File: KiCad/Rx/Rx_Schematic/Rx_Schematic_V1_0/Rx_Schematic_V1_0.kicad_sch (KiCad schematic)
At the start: 5 parts, among them J1 Analog, J2 Digital

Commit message: Updated schematic
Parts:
- removed J1: Analog, Connector_PinHeader_2.54mm:PinHeader_1x17_P2.54mm_Vertical, symbol Connector_Generic:Conn_01x17
- removed J2: Digital, Connector_PinHeader_2.54mm:PinHeader_1x17_P2.54mm_Vertical, symbol Connector_Generic:Conn_01x17
- added U?: ProMicro, symbol promicro:ProMicro
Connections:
- net at U?.1 (GND): now also U?.1 (GND), U?.23 (GND)
- net at U?.2 (VO): now also U?.2 (VCC)
- net at U?.3 (VI): now also U?.19 (F5)
- net at U?.3 (CE): now also U?.18 (F6)
- net at U?.4 (~{CSN}): now also U?.17 (F7)
- net at U?.5 (SCK): now also U?.16 (B1)
- net at U?.6 (MOSI): now also U?.14 (B2)
- net at U?.7 (MISO): now also U?.15 (B3)
- no-connect marks 2 -> 0
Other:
- moved on the sheet: U?

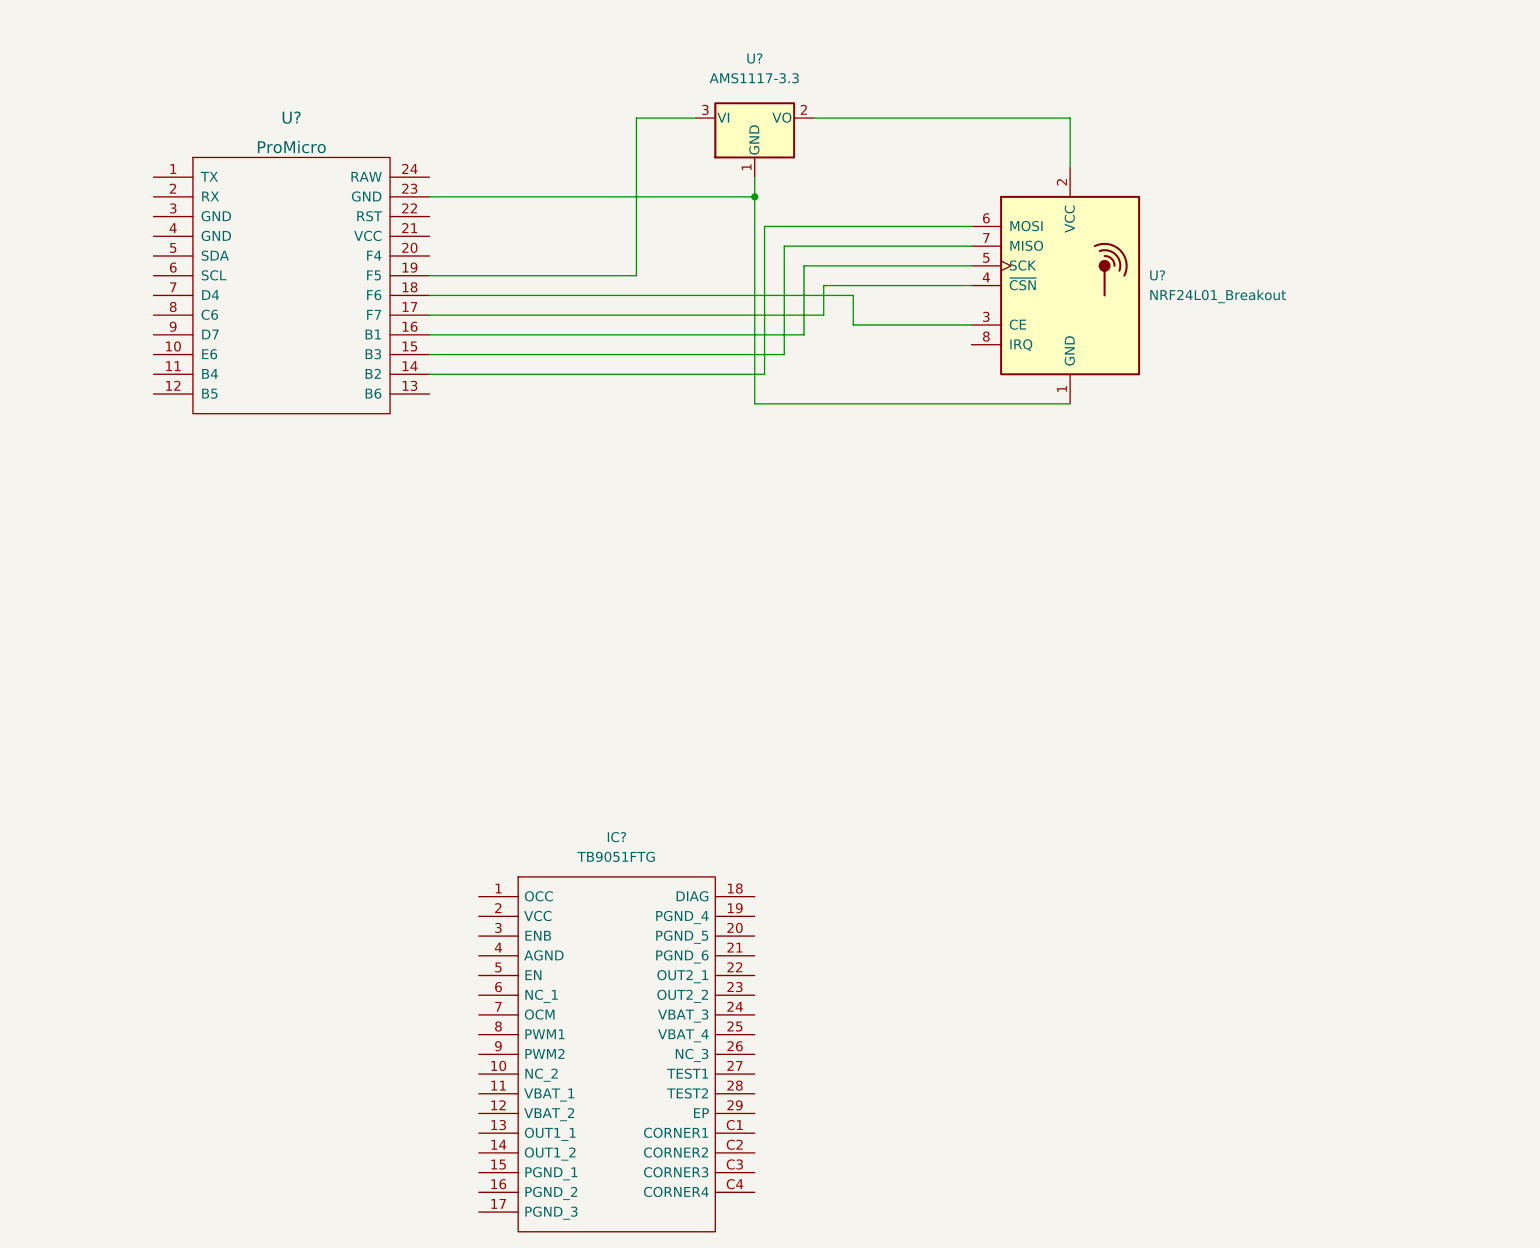
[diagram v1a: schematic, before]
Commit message: Updated Rx schematic
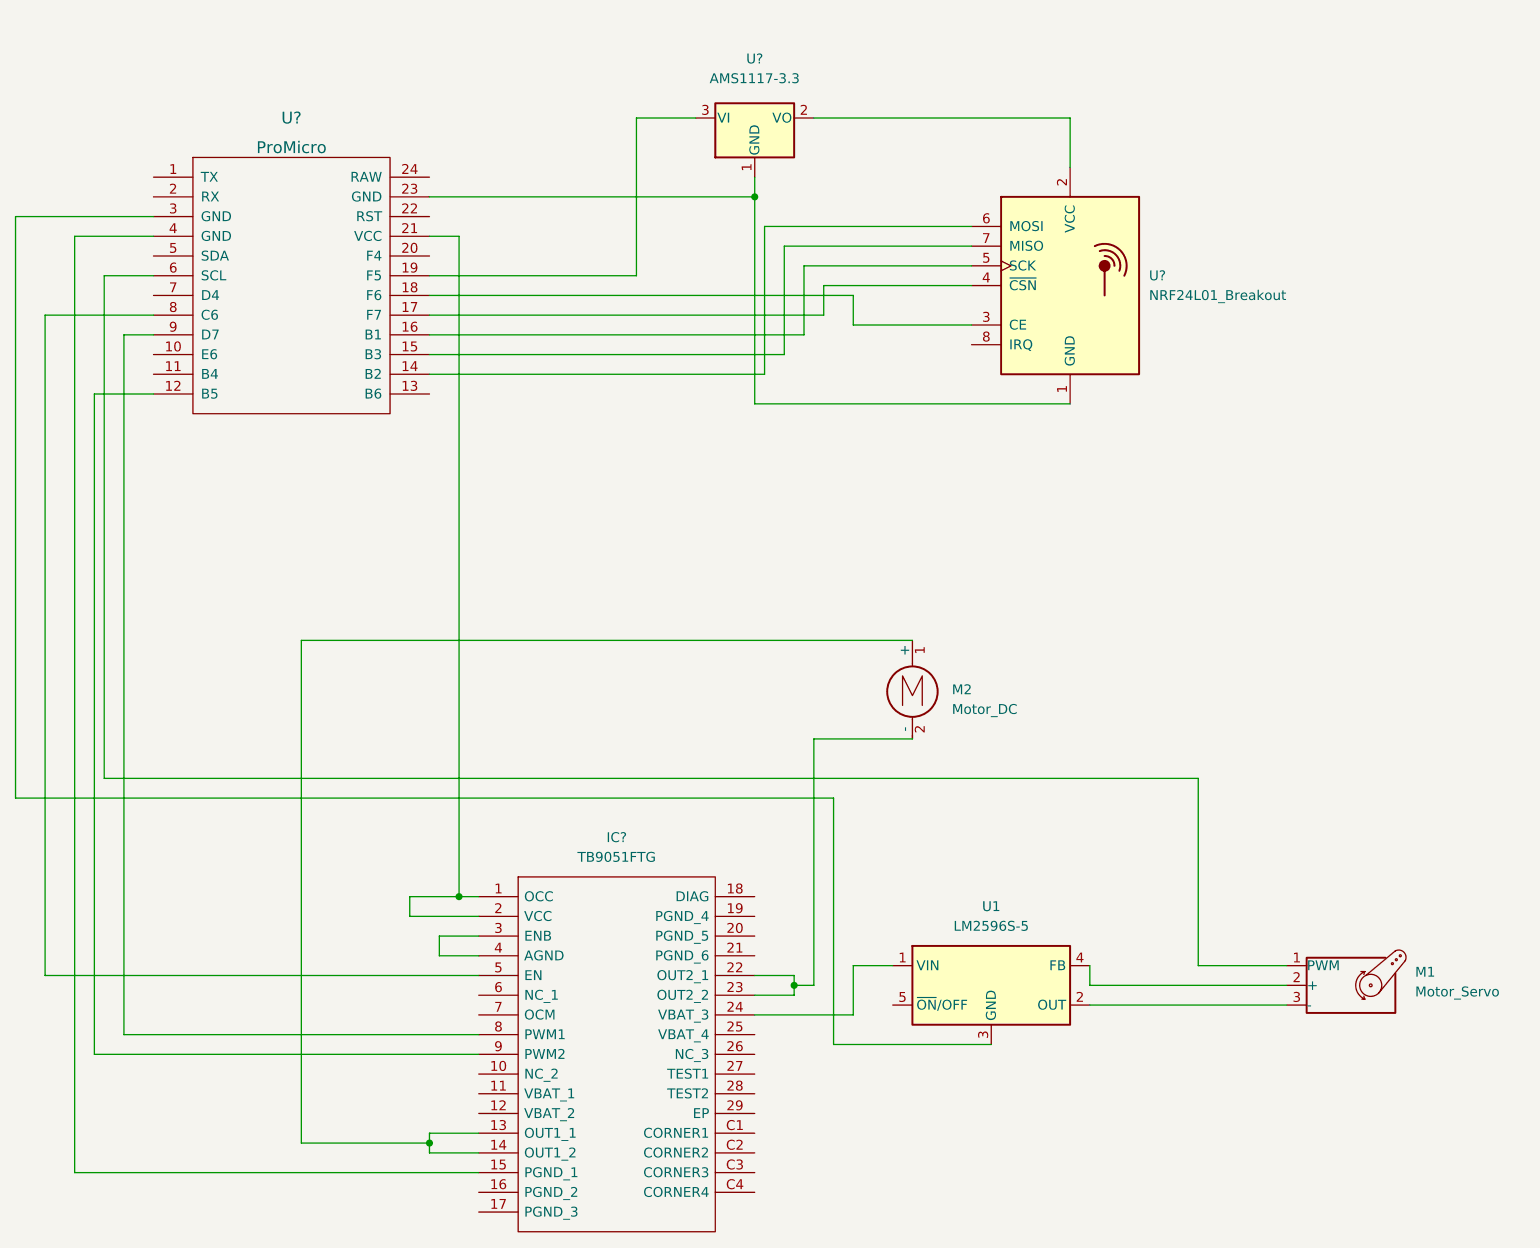
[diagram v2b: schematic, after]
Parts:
- added M1: Motor_Servo, symbol Motor:Motor_Servo
- added M2: Motor_DC, symbol Motor:Motor_DC
- added U1: LM2596S-5, Package_TO_SOT_SMD:TO-263-5_TabPin3, symbol Regulator_Switching:LM2596S-5
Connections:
- net at U?.12 (B5): now also IC?.9 (PWM2)
- net at U?.21 (VCC): now also IC?.1 (OCC), IC?.2 (VCC)
- net at U?.3 (GND): now also U1.3 (GND)
- net at U?.4 (GND): now also IC?.15 (PGND_1)
- net at U?.6 (SCL): now also M1.1 (PWM)
- net at U?.8 (C6): now also IC?.5 (EN)
- net at U?.9 (D7): now also IC?.8 (PWM1)
- net at IC?.13 (OUT1_1): now also IC?.14 (OUT1_2), M2.1 (+)
- net at IC?.22 (OUT2_1): now also IC?.23 (OUT2_2), M2.2 (-)
- net at IC?.24 (VBAT_3): now also U1.1 (VIN)
- net at IC?.3 (ENB): now also IC?.4 (AGND)
- new net: M1.3 (-), U1.2 (OUT)
- new net: M1.2 (+), U1.4 (FB)
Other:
- company: (none) -> David Duronslet
- title: (none) -> RC Car Rx V1_0

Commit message: Started new drawing
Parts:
- added J1: Conn_01x07, symbol Connector_Generic:Conn_01x07
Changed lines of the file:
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@@
+    )
+  )
+  (symbol (lib_id "Connector_Generic:Conn_01x07") (at 140.97 76.2 0) (unit 1)
+    (in_bom yes) (on_board yes) (dnp no) (fields_autoplaced)
+    (property "Reference" "J1" (at 143.51 74.93 0)
+      (effects (font (size 1.27 1.27)) (justify left))
+    )
+    (property "Value" "Conn_01x07" (at 143.51 77.47 0)
+      (effects (font (size 1.27 1.27)) (justify left))
+    )
+    (property "Footprint" "" (at 140.97 76.2 0)
+      (effects (font (size 1.27 1.27)) hide)
+    )
+    (property "Datasheet" "~" (at 140.97 76.2 0)
+      (effects (font (size 1.27 1.27)) hide)
+    )
+    (pin "1")
+    (pin "2")
+    (pin "3")
+    (pin "4")
+    (pin "5")
+    (pin "6")
+    (pin "7")
+    (instances
+      (project "Rx_Schematic_V1_0"
+        (path "/e63e39d7-6ac0-4ffd-8aa3-1841a4541b55"
+          (reference "J1") (unit 1)
+        )
+      )
     )
   )
